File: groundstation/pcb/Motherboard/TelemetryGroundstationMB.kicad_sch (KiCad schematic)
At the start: 122 parts, among them J1 USB-C, J10 Conn_01x01, J11 Conn_01x01, J12 USB-C, J2 USB-C, J3 ICD15S13E4GV00LF, J4 USB-C, J5 ICD15S13E4GV00LF, J6 ICD15S13E4GV00LF, J7 ICD15S13E4GV00LF, J8 LD09S33E4GV00LF, J9 Conn_01x04_Socket, M1 M4 Mounting Hole, M2 M4 Mounting Hole, M3 M4 Mounting Hole, M4 M4 Mounting Hole, SW1 SW_Push, SW2 SW_Push, SW3 SW_Push, SW4 SW_Push, SW5 SW_Push, SW6 SW_Push, SW7 SW_Push, SW8 SW_DIP_x01, U1 CP2102N, U2 CP2102N, U3 CP2102N, U5 AVR128DB64x-xPT, U6 MIC29300-3.3WU-TR

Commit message: improve component 3d models
also update pcb 3d models and renderings. fixes #35
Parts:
- J11: footprint Footprints:Banana_CT3151-0 -> Footprints:Banana_CT3151-2
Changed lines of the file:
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@@
 			)
 		)
-		(property "Footprint" "Footprints:Banana_CT3151-0"
+		(property "Footprint" "Footprints:Banana_CT3151-2"
 			(at 511.81 322.58 0)
 			(effects

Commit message: add drawing sheet informations
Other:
- company: (none) -> Spaceflight Rocketry Giessen e.V.
- title: (none) -> Telemetry Groundstation Motherboard PCB
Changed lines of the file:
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@@
 	(generator_version "9.0")
 	(paper "A2")
+	(title_block
+		(title "Telemetry Groundstation Motherboard PCB")
+		(date "2026-03-01")
+		(company "Spaceflight Rocketry Giessen e.V.")
+	)
 	(rectangle
 		(start 481.33 90.17)

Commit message: add Digikey purchase links for Daughter- and Motherboard
fixes #30
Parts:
- C1, C3, C6: value 4.7 uF -> 4.7u; Purchase-URL (none) -> https://www.digikey.de/de/products/detail/samsung-electro-m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
- C10, C11, C12, C9: value 1 uF -> 1u; Purchase-URL https://www.digikey.de/de/products/detail/samsung-electro-mechanics/CL21B105KAFNNNE/3886724 -> https://www.digikey.de/de/products/detail/samsung-electro-mechanics/CL21B105KBFNNNE/3886687
- C13: value 100uF Elko -> 100u Elko; Purchase-URL (none) -> https://www.digikey.de/en/products/detail/elna-america/RSRC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
- C2, C4, C5: value 0.1 uF -> 0.1u; Purchase-URL (none) -> https://www.digikey.de/de/products/detail/samsung-electro-m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
- C7: value 10uF Tantal -> 10u Tantal; Purchase-URL (none) -> https://www.digikey.de/en/products/detail/kyocera-avx/TAJA1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
- D1, D16, D2, D3, D7: Purchase-URL (none) -> https://www.digikey.de/de/products/detail/liteon/LTST-C170K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
- D10: Purchase-URL (none) -> https://www.digikey.de/en/products/detail/mcc-micro-commerc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
- D11, D12, D15, D6, D9: Purchase-URL (none) -> https://www.digikey.de/de/products/detail/liteon/LTST-C171K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
- D13: Purchase-URL (none) -> https://www.digikey.de/en/products/detail/w%C3%BCrth-elektr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
- D14, D5, D8: Purchase-URL (none) -> https://www.digikey.de/en/products/detail/littelfuse-inc/SP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
- D4: Purchase-URL (none) -> https://www.digikey.de/de/products/detail/cree-led/CLP6C-FK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
- J1, J12, J2, J4: Purchase-URL (none) -> https://www.digikey.de/en/products/detail/gct/USB4216-03-A/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
- J3, J5, J6, J7: Purchase-URL (none) -> https://www.digikey.de/en/products/detail/amphenol-cs-fci/I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
- J8: Purchase-URL (none) -> https://www.digikey.de/en/products/detail/amphenol-cs-fci/L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
- R1, R11, R12, R17, R2, R20, R21, R25, R26, R3, R37, R4, R5, R6: value 560 Ohm -> 560R; Purchase-URL (none) -> https://www.digikey.de/de/products/detail/stackpole-electro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
- R10, R13, R14, R15, R16, R22, R23, R24, R27, R28, R29, R30, R31, R32, R33, R34, R35, R36, R38, R39, R40, R41, R7, R8, R9: Purchase-URL (none) -> https://www.digikey.de/en/products/detail/stackpole-electro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
- R18, R19: value 470 Ohm -> 470R; Purchase-URL (none) -> https://www.digikey.de/en/products/detail/stackpole-electro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
- R47, R48, R51, R52, R53, R54, R55, R56: value 560 Ohm -> 560R; Purchase-URL https://www.digikey.de/de/products/detail/yageo/RC0805JR-07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 -> https://www.digikey.de/de/products/detail/stackpole-electro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
- U1, U2, U3: Purchase-URL (none) -> https://www.digikey.de/en/products/detail/silicon-labs/CP21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
- U6: Purchase-URL (none) -> https://www.digikey.de/en/products/detail/microchip-technol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

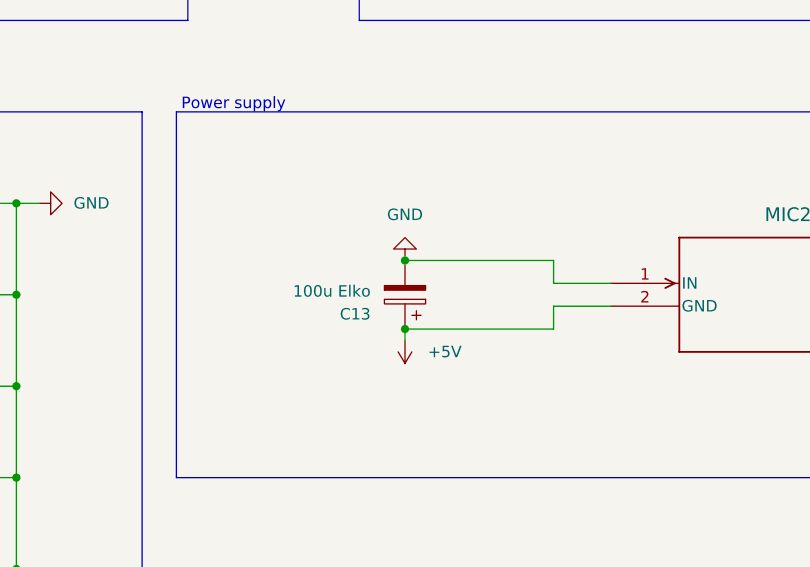
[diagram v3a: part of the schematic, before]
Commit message: fix 3D Models and rearrange wires. Fixes #46
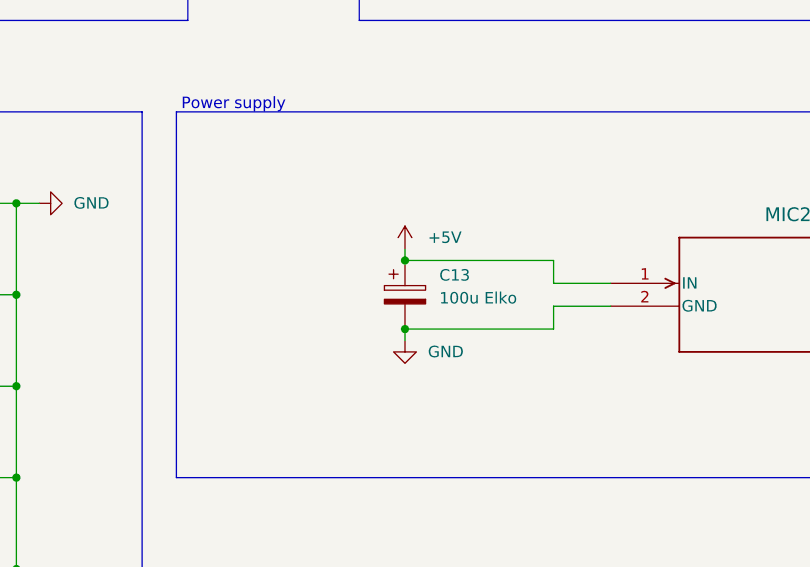
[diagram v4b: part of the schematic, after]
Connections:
- net +5V: now also U6.1 (IN); no longer U6.2 (GND)
- net GND: now also U6.2 (GND); no longer U6.1 (IN)
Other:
- moved on the sheet: C13
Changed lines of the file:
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@@
 	)
 	(junction
-		(at 170.18 322.58)
-		(diameter 0)
-		(color 0 0 0 0)
-	)
-	(junction
 		(at 127 316.23)
 		(diameter 0)
@@
 	)
 	(junction
+		(at 170.18 322.58)
+		(diameter 0)
+		(color 0 0 0 0)
+	)
+	(junction
 		(at 107.95 184.15)
 		(diameter 0)
@@
 	)
 	(junction
-		(at 170.18 330.2)
-		(diameter 0)
-		(color 0 0 0 0)
-	)
-	(junction
 		(at 49.53 201.93)
 		(diameter 0)
@@
 	)
 	(junction
+		(at 170.18 330.2)
+		(diameter 0)
+		(color 0 0 0 0)
+	)
+	(junction
 		(at 251.46 186.69)
 		(diameter 0)
@@
 	(wire
 		(pts
+			(xy 170.18 331.47) (xy 170.18 330.2)
+		)
+		(stroke
+			(width 0)
+			(type default)
+		)
+	)
+	(wire
+		(pts
 			(xy 114.3 367.03) (xy 116.84 367.03)
 		)
@@
 	(wire
 		(pts
+			(xy 170.18 321.31) (xy 170.18 322.58)
+		)
+		(stroke
+			(width 0)
+			(type default)
+		)
+	)
+	(wire
+		(pts
 			(xy 210.82 77.47) (xy 220.98 77.47)
 		)
@@
 	(wire
 		(pts
-			(xy 170.18 331.47) (xy 170.18 330.2)
-		)
-		(stroke
-			(width 0)
-			(type default)
-		)
-	)
-	(wire
-		(pts
 			(xy 486.41 171.45) (xy 486.41 173.99)
 		)
@@
 	(symbol
 		(lib_id "power:+BATT")
-		(at 170.18 331.47 180)
+		(at 170.18 321.31 0)
 		(unit 1)
 		(exclude_from_sim no)
@@
 		(fields_autoplaced yes)
 		(property "Reference" "#PWR0134"
-			(at 170.18 327.66 0)
+			(at 170.18 325.12 0)
 			(effects
 				(font
@@
 		)
 		(property "Value" "+5V"
-			(at 172.72 332.7399 0)
+			(at 172.72 320.0399 0)
 			(effects
 				(font
 					(size 1.27 1.27)
 				)
-				(justify right)
+				(justify left)
 			)
 		)
 		(property "Footprint" ""
-			(at 170.18 331.47 0)
+			(at 170.18 321.31 0)
 			(effects
 				(font
@@
 		)
 		(property "Datasheet" ""
-			(at 170.18 331.47 0)
+			(at 170.18 321.31 0)
 			(effects
 				(font
@@
 		)
 		(property "Description" "Power symbol creates a global label with name \"+BATT\""
-			(at 170.18 331.47 0)
+			(at 170.18 321.31 0)
 			(effects
 				(font
@@
 		(lib_name "GND_2")
 		(lib_id "power:GND")
-		(at 170.18 322.58 180)
+		(at 170.18 331.47 0)
 		(unit 1)
 		(exclude_from_sim no)
@@
 		(fields_autoplaced yes)
 		(property "Reference" "#PWR0135"
-			(at 170.18 316.23 0)
+			(at 170.18 337.82 0)
 			(effects
 				(font
@@
 		)
 		(property "Value" "GND"
-			(at 170.18 317.5 0)
+			(at 172.72 332.7399 0)
 			(effects
 				(font
 					(size 1.27 1.27)
 				)
+				(justify left)
 			)
 		)
 		(property "Footprint" ""
-			(at 170.18 322.58 0)
+			(at 170.18 331.47 0)
 			(effects
 				(font
@@
 		)
 		(property "Datasheet" ""
-			(at 170.18 322.58 0)
+			(at 170.18 331.47 0)
 			(effects
 				(font
@@
 		)
 		(property "Description" "Power symbol creates a global label with name \"GND\" , ground"
-			(at 170.18 322.58 0)
+			(at 170.18 331.47 0)
 			(effects
 				(font
@@
 	(symbol
 		(lib_id "Device:C_Polarized")
-		(at 170.18 326.39 180)
+		(at 170.18 326.39 0)
 		(unit 1)
 		(exclude_from_sim no)
@@
 		(fields_autoplaced yes)
 		(property "Reference" "C13"
-			(at 166.37 328.5491 0)
+			(at 173.99 324.2309 0)
 			(effects
 				(font
@@
 		)
 		(property "Value" "100u Elko"
-			(at 166.37 326.0091 0)
+			(at 173.99 326.7709 0)
 			(effects
 				(font
@@
 		)
 		(property "Footprint" "Capacitor_THT:CP_Radial_D6.3mm_P2.50mm"
-			(at 169.2148 322.58 0)
+			(at 171.1452 330.2 0)
 			(effects
 				(font
